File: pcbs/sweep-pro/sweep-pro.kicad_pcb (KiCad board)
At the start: 2 copper layers, 115 x 90 mm, 41 parts, among them SW1 SW_PUSH-kbd, SW10 SW_PUSH-kbd, SW11 SW_PUSH-kbd, SW12 SW_PUSH-kbd, SW13 SW_PUSH-kbd, SW14 SW_PUSH-kbd, SW15 SW_PUSH-kbd, SW16 SW_PUSH-kbd, SW17 SW_PUSH-kbd, SW2 SW_PUSH-kbd, SW3 SW_PUSH-kbd, SW4 SW_PUSH-kbd, SW5 SW_PUSH-kbd, SW6 SW_PUSH-kbd, SW7 SW_PUSH-kbd, SW8 SW_PUSH-kbd, SW9 SW_PUSH-kbd, U1 ProMicro-kbd

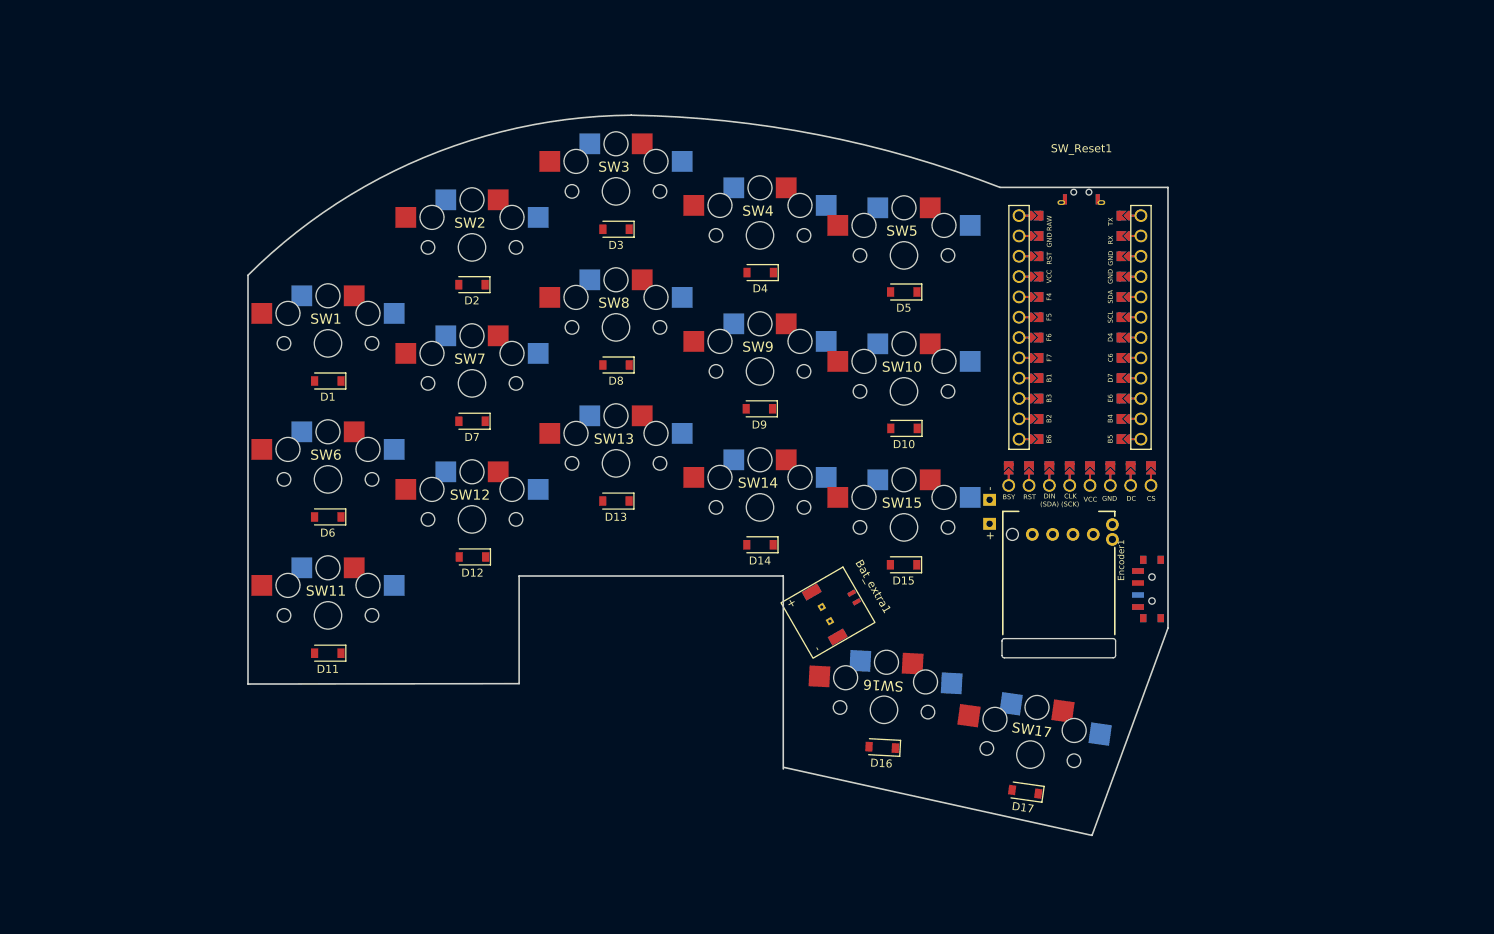
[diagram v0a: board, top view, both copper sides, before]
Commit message: first version with complete routing
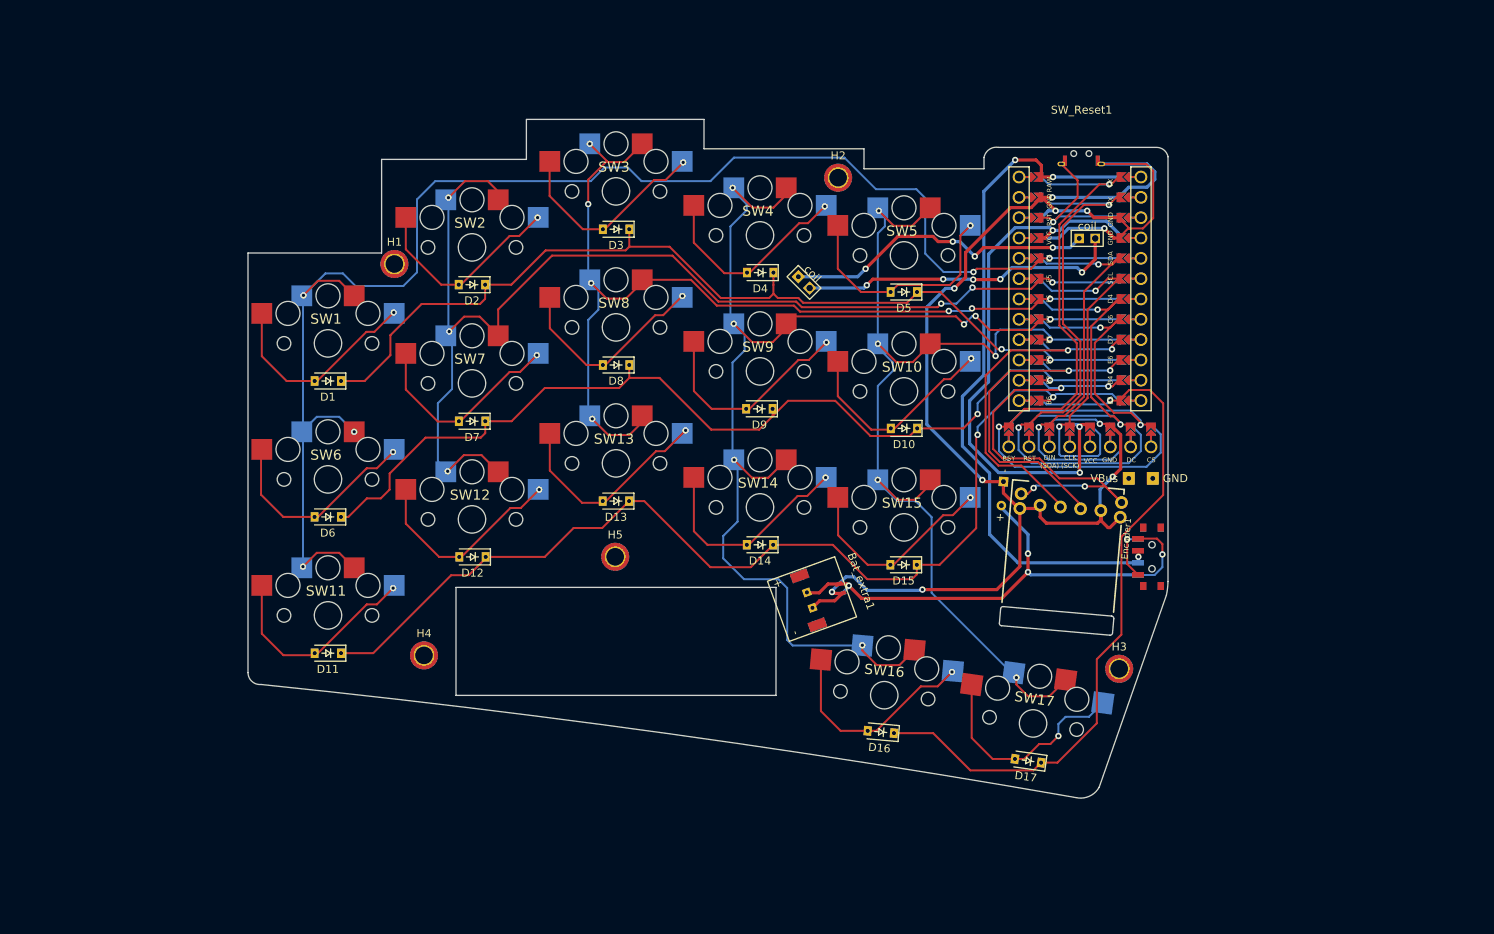
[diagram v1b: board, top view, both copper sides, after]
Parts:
- added Coil_input1: Conn_01x02_Female, mylib:WirelessChager_pads_reversible, F.Cu at (166.5, 59.4)
- added Coil_output1: Conn_01x02_Female, mylib:WirelessChager_pads_reversible, F.Cu at (201.9, 53.9)
- added H1: MountingHole, MountingHole:MountingHole_2.2mm_M2_ISO7380_Pad_TopBottom, F.Cu at (115.3, 57.1)
- added H2: MountingHole, MountingHole:MountingHole_2.2mm_M2_ISO7380_Pad_TopBottom, F.Cu at (170.8, 46.3)
- added H3: MountingHole, MountingHole:MountingHole_2.2mm_M2_ISO7380_Pad_TopBottom, F.Cu at (205.9, 107.7)
- added H4: MountingHole, MountingHole:MountingHole_2.2mm_M2_ISO7380_Pad_TopBottom, F.Cu at (119.0, 106.0)
- added H5: MountingHole, MountingHole:MountingHole_2.2mm_M2_ISO7380_Pad_TopBottom, F.Cu at (142.9, 93.7)
- added Vbus_con1: Conn_01x02_Female, mylib:VBus_pad_reversible, F.Cu at (208.6, 83.9)
- Bat_main1: moved to B.Cu
- D1, D10, D11, D12, D13, D14, D15, D16, D17, D2, D3, D4, D5, D6, D7, D8, D9: footprint Diode_SMD:D_SOD-123 -> mylib:Diode_SOD-123_reversible
- Encoder1: footprint mylib:RollerEncoder_Panasonic_EVQWGD001 -> mylib:RollerEncoder_EVQWGD001_reversible
- moved U1 4.83 mm to (201.0, 60.2)
- moved SW_Reset1 4.82 mm to (201.2, 42.4)
- moved Display1 4.82 mm to (201.0, 79.3)
- moved SW_Power1 4.03 mm to (210.0, 93.7)
- moved SW17 3.91 mm to (195.1, 114.5)
- moved D17 3.89 mm to (194.5, 119.2)
- moved Encoder1 3.37 mm to (199.3, 93.2), turned to -95 degrees
- moved Bat_main1 2.78 mm to (191.3, 85.8), turned to 85 degrees
- moved Bat_extra1 2.54 mm to (168.0, 98.8), turned to -70 degrees
- moved D16 1.93 mm to (176.1, 115.6), turned to 175 degrees
- moved SW16 1.83 mm to (176.5, 111.0), turned to -5 degrees
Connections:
- U1 pad 10: encoder_b -> encoder_a
- U1 pad 9: encoder_a -> encoder_b
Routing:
- net GND: track 0.00 -> 197.5 mm, vias 0 -> 10
- net col1: track 0.00 -> 186.4 mm, vias 0 -> 5
- net col4: track 0.00 -> 155.4 mm, vias 0 -> 7
- net col2: track 0.00 -> 149.6 mm, vias 0 -> 6
- net col5: track 0.00 -> 133.4 mm, vias 0 -> 6
- net row3: track 0.00 -> 131.8 mm, vias 0 -> 2
- net col3: track 0.00 -> 122.2 mm, vias 0 -> 7
- net row2: track 0.00 -> 121.0 mm, vias 0 -> 2
- net row1: track 0.00 -> 120.3 mm, vias 0 -> 2
- net row4: track 0.00 -> 90.0 mm, vias 0 -> 1
- net VRaw: track 0.00 -> 87.2 mm, vias 0 -> 3
- net bsy: track 0.00 -> 81.0 mm, vias 0 -> 2
- net rst: track 0.00 -> 72.0 mm, vias 0 -> 2
- net VCC: track 0.00 -> 69.7 mm, vias 0 -> 3
- net VBat: track 0.00 -> 64.8 mm, vias 0 -> 4
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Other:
- board size 115 x 90 mm -> 115 x 84.8 mm

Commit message: outline and routing finished
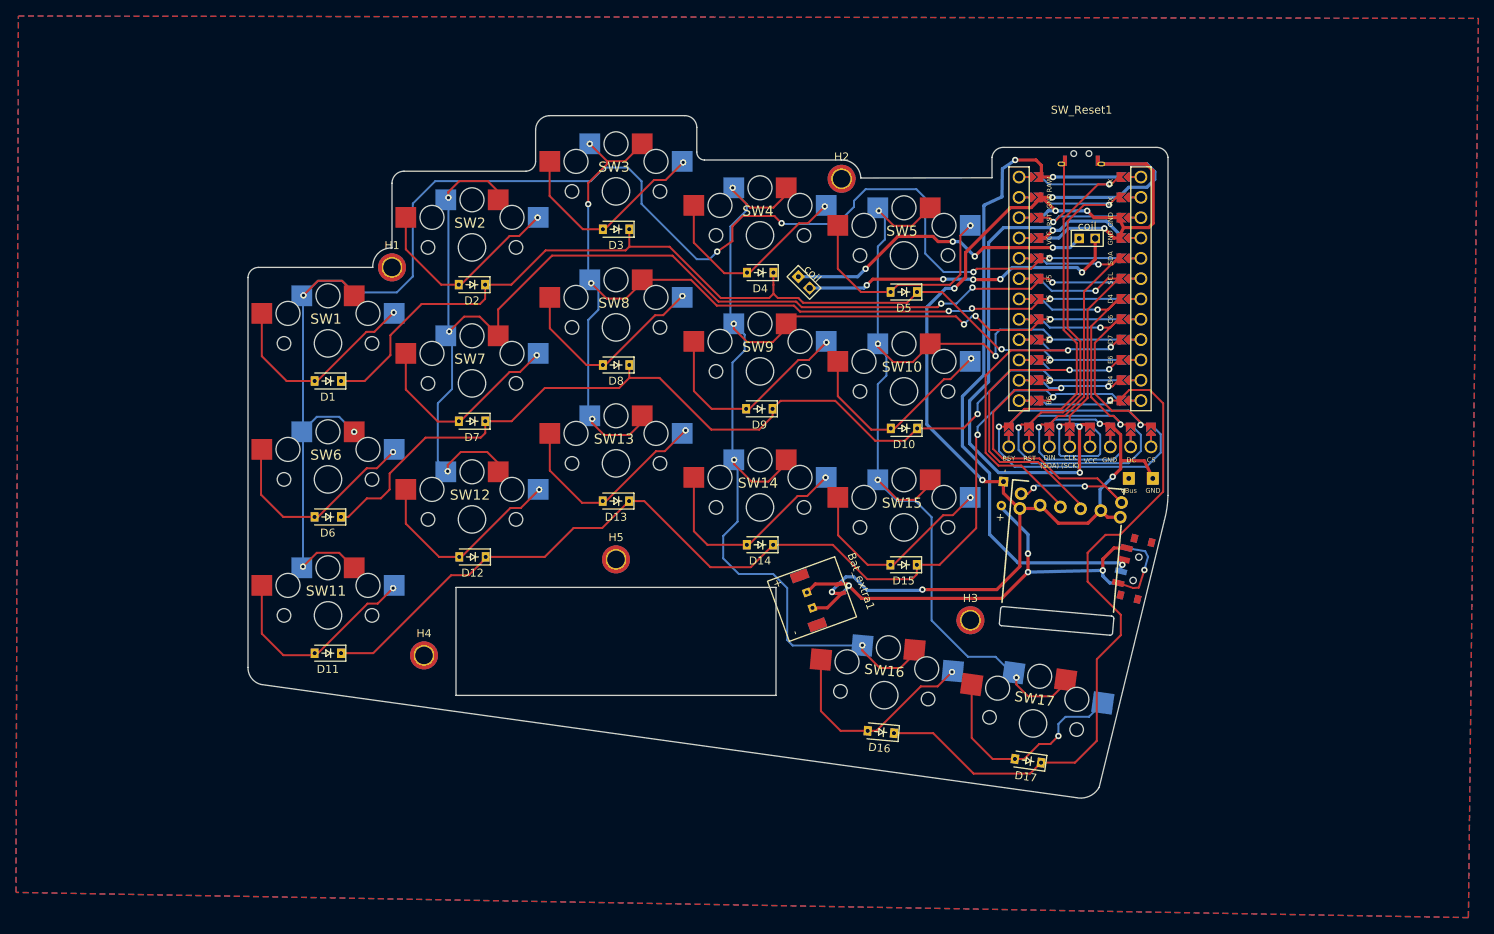
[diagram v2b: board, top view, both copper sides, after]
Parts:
- SW_Power1: value SW_Battery_kbd -> SW_Battery-kbd
- moved H3 19.6 mm to (187.3, 101.6)
- moved SW_Power1 2.50 mm to (208.0, 95.2), turned to 76.2 degrees
- moved H1 0.52 mm to (115.0, 57.5)
- moved H2 0.45 mm to (171.2, 46.4)
- moved H5 0.34 mm to (143.0, 94.0)
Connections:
- Vbus_con1 pad gnd: unconnected-(Vbus_con1-Padgnd) -> GND
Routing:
- net col1: track 186.4 -> 195.2 mm, vias 5 -> 7
- net VBat: track 64.8 -> 58.5 mm
- net row4: track 90.0 -> 96.2 mm
- net unconnected-(SW_Power1-Pad1): track 6.38 -> 9.84 mm
- net GND: track 197.5 -> 199.7 mm
- net col4: track 155.4 -> 157.5 mm
- net col2: track 149.6 -> 151.4 mm
- net col5: track 133.4 -> 135.2 mm
- net reset: track 20.2 -> 18.9 mm
- net VRaw: track 87.2 -> 86.0 mm
- net VCC: track 69.7 -> 70.6 mm
- added copper zone on B.Cu, net GND
- added copper zone on F.Cu, net GND
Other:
- board size 115 x 84.8 mm -> 115 x 85.3 mm
